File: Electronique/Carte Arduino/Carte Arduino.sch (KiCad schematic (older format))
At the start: 2 parts

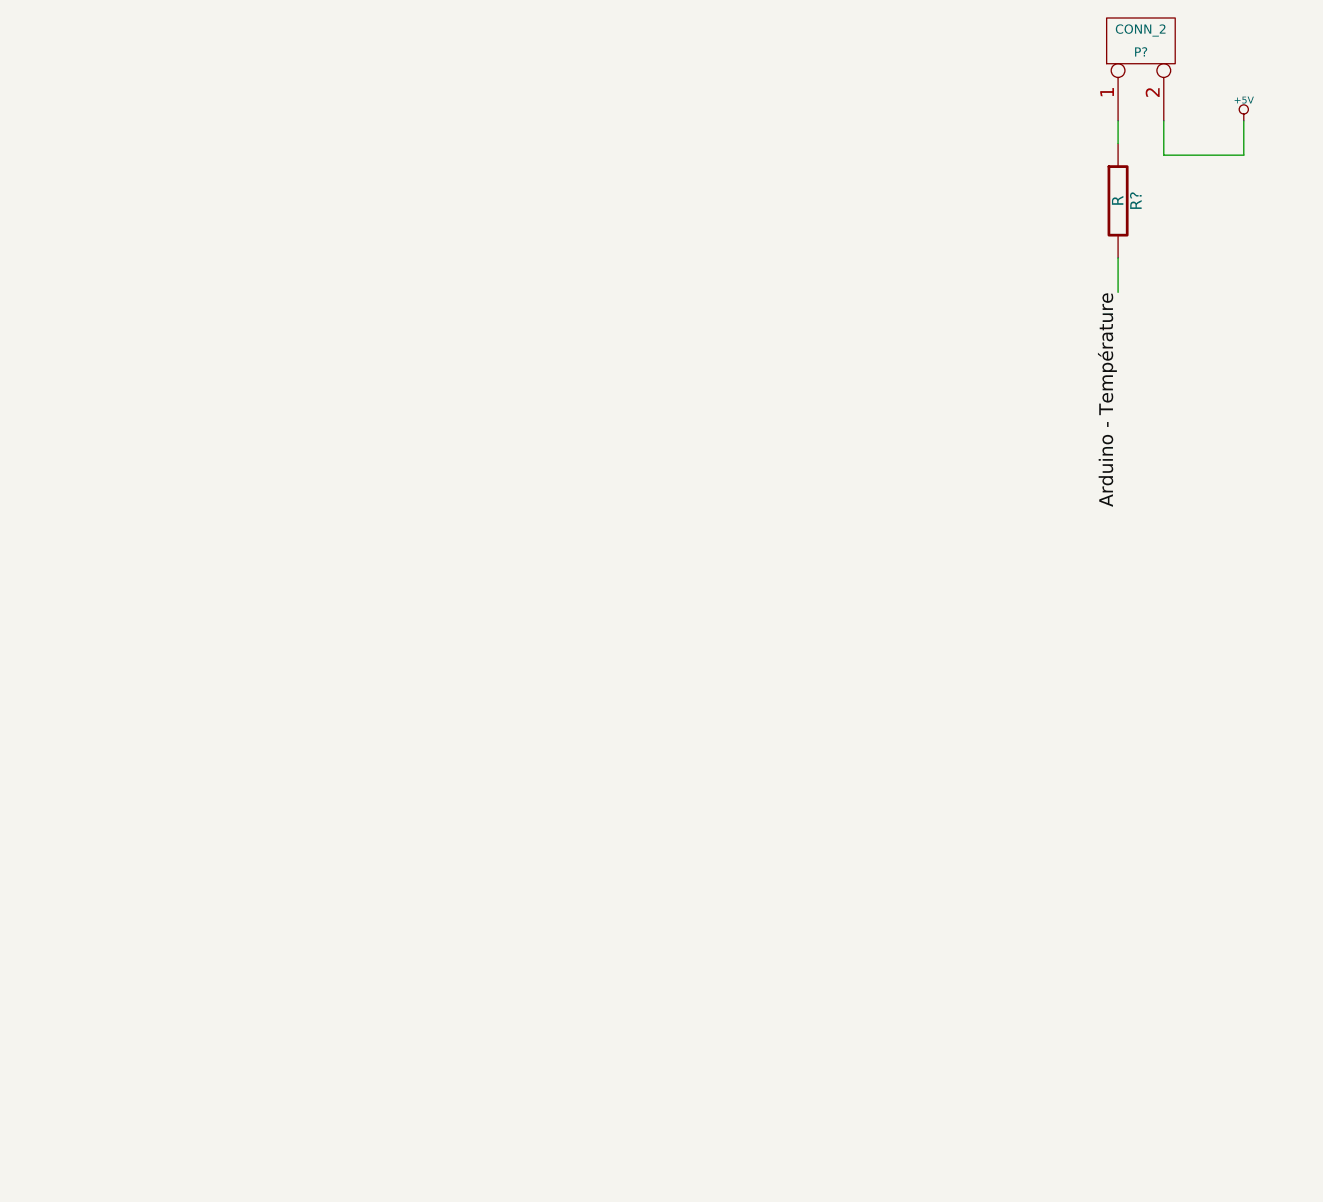
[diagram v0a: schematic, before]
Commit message: Electronique/Carte Arduino/Carte Arduino.sch : - Ajout du capteur de pression
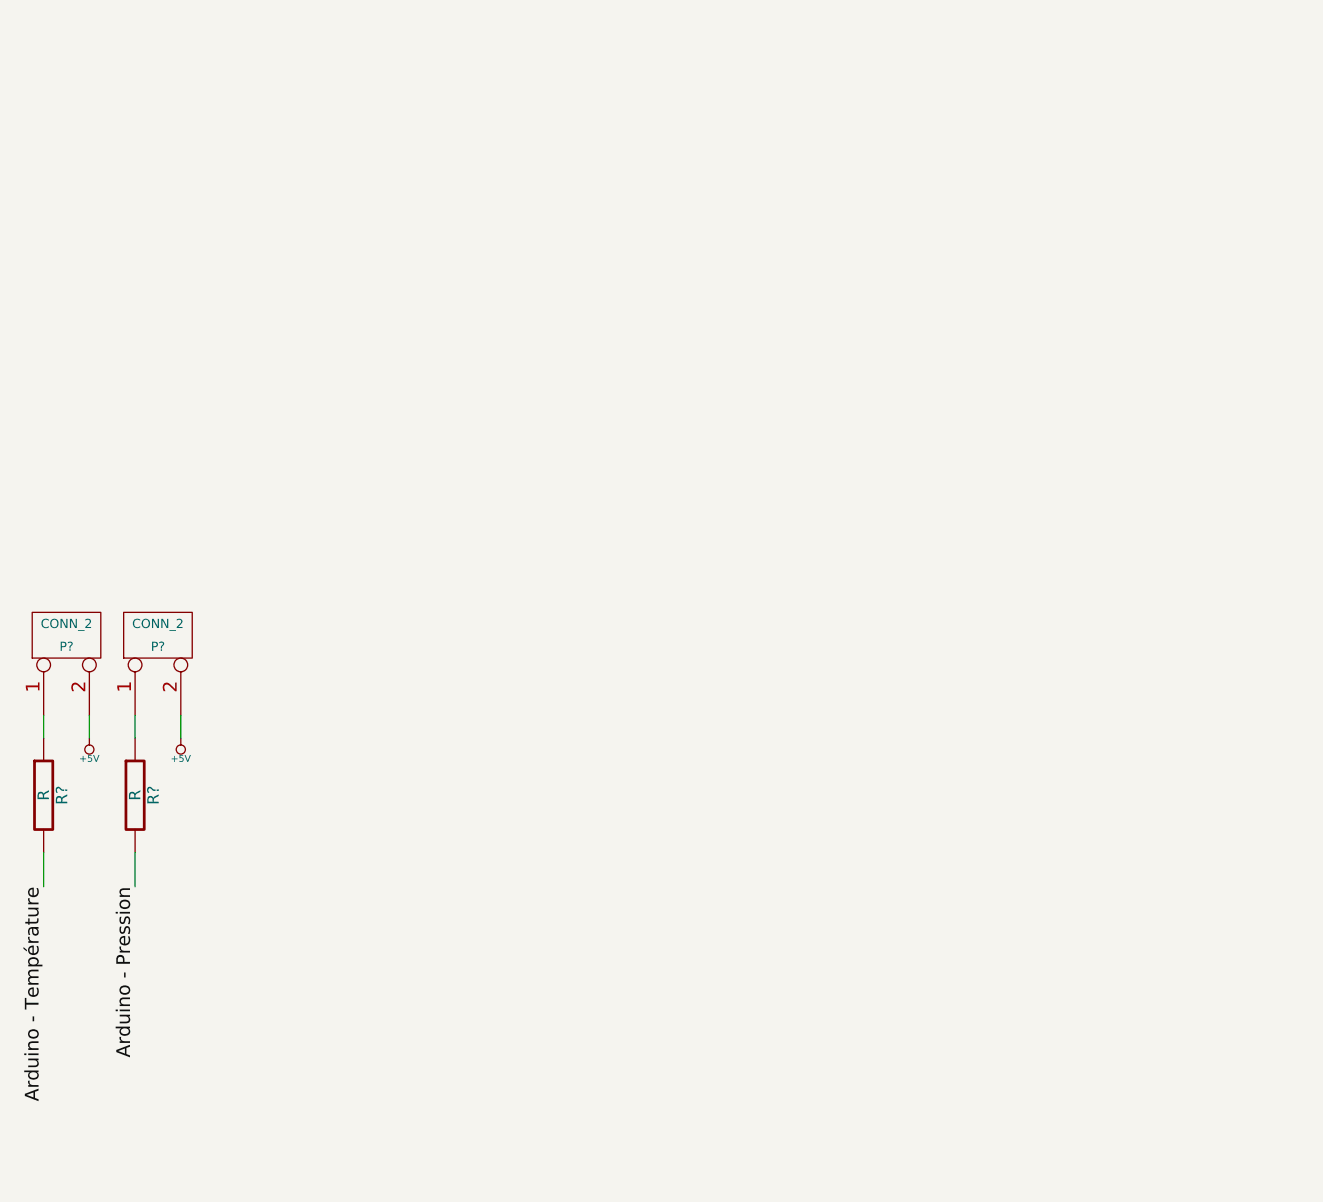
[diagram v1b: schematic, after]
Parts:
- added P?: CONN_2, symbol CONN_2
- added R?: R, symbol R
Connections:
- net +5V: now also P?.2 (PM)
- new net: P?.1 (P1), R?.1
- new net Arduino - Pression: R?.2
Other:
- moved on the sheet: P?, R?
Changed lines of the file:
@@
-EESchema Schematic File Version 2  date 09/12/2011 07:44:42
+EESchema Schematic File Version 2  date 09/12/2011 16:36:29
 LIBS:power
 LIBS:device
@@
 $EndDescr
 Wire Wire Line
-	5550 3450 5550 3600
+	1250 6050 1250 6200
 Wire Wire Line
-	5750 2850 5750 3000
+	1250 5450 1250 5550
 Wire Wire Line
-	5750 3000 6100 3000
+	1450 5550 1450 5450
 Wire Wire Line
-	6100 3000 6100 2850
+	1050 5550 1050 5450
 Wire Wire Line
-	5550 2850 5550 2950
+	850  5450 850  5550
+Wire Wire Line
+	850  6050 850  6200
+$Comp
+L +5V #PWR?
+U 1 1 4EE22ACD
+P 1450 5550
+F 0 "#PWR?" H 1450 5640 20  0001 C CNN
+F 1 "+5V" H 1450 5640 30  0000 C CNN
+	1    1450 5550
+	-1   0    0    1
+$EndComp
+$Comp
+L CONN_2 P?
+U 1 1 4EE22ACC
+P 1350 5100
+F 0 "P?" V 1300 5100 40  0000 C CNN
+F 1 "CONN_2" V 1400 5100 40  0000 C CNN
+	1    1350 5100
+	0    -1   -1   0
+$EndComp
+Text Label 1250 6200 3    60   ~ 0
+Arduino - Pression
+$Comp
+L R R?
+U 1 1 4EE22ACB
+P 1250 5800
+F 0 "R?" V 1330 5800 50  0000 C CNN
+F 1 "R" V 1250 5800 50  0000 C CNN
+	1    1250 5800
+	1    0    0    -1
+$EndComp
 $Comp
 L R R?
 U 1 1 4EE1ADE8
-P 5550 3200
-F 0 "R?" V 5630 3200 50  0000 C CNN
-F 1 "R" V 5550 3200 50  0000 C CNN
-	1    5550 3200
+P 850 5800
+F 0 "R?" V 930 5800 50  0000 C CNN
+F 1 "R" V 850 5800 50  0000 C CNN
+	1    850  5800
 	1    0    0    -1
 $EndComp
-Text Label 5550 3600 3    60   ~ 0
+Text Label 850  6200 3    60   ~ 0
 Arduino - Température
 $Comp
 L CONN_2 P?
 U 1 1 4EE1AD34
-P 5650 2500
-F 0 "P?" V 5600 2500 40  0000 C CNN
-F 1 "CONN_2" V 5700 2500 40  0000 C CNN
-	1    5650 2500
+P 950 5100
+F 0 "P?" V 900 5100 40  0000 C CNN
+F 1 "CONN_2" V 1000 5100 40  0000 C CNN
+	1    950  5100
 	0    -1   -1   0
 $EndComp
@@
 L +5V #PWR?
 U 1 1 4EE0BB2B
-P 6100 2850
-F 0 "#PWR?" H 6100 2940 20  0001 C CNN
-F 1 "+5V" H 6100 2940 30  0000 C CNN
-	1    6100 2850
-	1    0    0    -1
+P 1050 5550
+F 0 "#PWR?" H 1050 5640 20  0001 C CNN
+F 1 "+5V" H 1050 5640 30  0000 C CNN
+	1    1050 5550
+	-1   0    0    1
 $EndComp
 $EndSCHEMATC

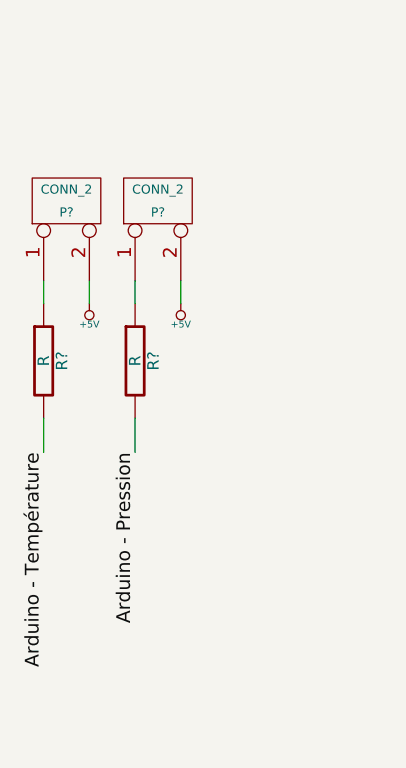
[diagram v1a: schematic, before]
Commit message: Electronique/Carte Arduino/Carte Arduino.pro : - Ajout des capteur de pression et de temperature interne
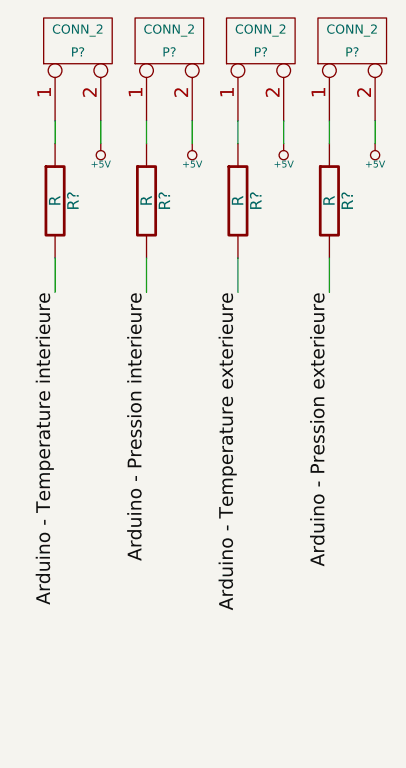
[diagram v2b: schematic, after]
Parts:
- added P? (x2): CONN_2, symbol CONN_2
- added R? (x2): R, symbol R
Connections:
- net +5V: now also P?.2 (PM), P?.2 (PM)
- net Arduino - Pression renamed Arduino - Pression interieure
- net Arduino - Température renamed Arduino - Temperature interieure
- new net: P?.1 (P1), R?.1 (x2)
- new net Arduino - Pression exterieure: R?.2
- new net Arduino - Temperature exterieure: R?.2
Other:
- moved on the sheet: P?, R?
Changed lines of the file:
@@
-EESchema Schematic File Version 2  date 09/12/2011 16:36:29
-LIBS:power
-LIBS:device
-LIBS:transistors
-LIBS:conn
-LIBS:linear
-LIBS:regul
-LIBS:74xx
-LIBS:cmos4000
-LIBS:adc-dac
-LIBS:memory
-LIBS:xilinx
-LIBS:special
-LIBS:microcontrollers
-LIBS:dsp
-LIBS:microchip
-LIBS:analog_switches
-LIBS:motorola
-LIBS:texas
-LIBS:intel
-LIBS:audio
-LIBS:interface
-LIBS:digital-audio
-LIBS:philips
-LIBS:display
-LIBS:cypress
-LIBS:siliconi
-LIBS:opto
-LIBS:atmel
-LIBS:contrib
-LIBS:valves
-LIBS:Carte Arduino-cache
-EELAYER 25  0
+EESchema Schematic File Version 1
+LIBS:power,device,conn,linear,regul,74xx,cmos4000,adc-dac,memory,xilinx,special,microcontrollers,dsp,microchip,analog_switches,motorola,texas,intel,audio,interface,digital-audio,philips,display,cypress,siliconi,contrib,valves
+EELAYER 23  0
 EELAYER END
 $Descr A4 11700 8267
-encoding utf-8
 Sheet 1 1
 Title ""
@@
 $EndDescr
 Wire Wire Line
-	1250 6050 1250 6200
+	2100 5350 2100 5500
 Wire Wire Line
-	1250 5450 1250 5550
+	2100 4750 2100 4850
 Wire Wire Line
-	1450 5550 1450 5450
+	2300 4850 2300 4750
 Wire Wire Line
-	1050 5550 1050 5450
+	1900 4850 1900 4750
 Wire Wire Line
-	850  5450 850  5550
+	1700 4750 1700 4850
 Wire Wire Line
-	850  6050 850  6200
+	1700 5350 1700 5500
+$Comp
+L +5V #PWR?
+U 1 1 4EE364FB
+P 2300 4850
+F 0 "#PWR?" H 2300 4940 20  0001 C C
+F 1 "+5V" H 2300 4940 30  0000 C C
+	1    2300 4850
+	-1   0    0    1
+$EndComp
+$Comp
+L CONN_2 P?
+U 1 1 4EE364FA
+P 2200 4400
+F 0 "P?" V 2150 4400 40  0000 C C
+F 1 "CONN_2" V 2250 4400 40  0000 C C
+	1    2200 4400
+	0    -1   -1   0
+$EndComp
+Text Label 2100 5500 3    60   ~
+Arduino - Pression exterieure
+$Comp
+L R R?
+U 1 1 4EE364F9
+P 2100 5100
+F 0 "R?" V 2180 5100 50  0000 C C
+F 1 "R" V 2100 5100 50  0000 C C
+	1    2100 5100
+	1    0    0    -1
+$EndComp
+$Comp
+L R R?
+U 1 1 4EE364F8
+P 1700 5100
+F 0 "R?" V 1780 5100 50  0000 C C
+F 1 "R" V 1700 5100 50  0000 C C
+	1    1700 5100
+	1    0    0    -1
+$EndComp
+Text Label 1700 5500 3    60   ~
+Arduino - Temperature exterieure
+$Comp
+L CONN_2 P?
+U 1 1 4EE364F7
+P 1800 4400
+F 0 "P?" V 1750 4400 40  0000 C C
+F 1 "CONN_2" V 1850 4400 40  0000 C C
+	1    1800 4400
+	0    -1   -1   0
+$EndComp
+$Comp
+L +5V #PWR?
+U 1 1 4EE364F6
+P 1900 4850
+F 0 "#PWR?" H 1900 4940 20  0001 C C
+F 1 "+5V" H 1900 4940 30  0000 C C
+	1    1900 4850
+	-1   0    0    1
+$EndComp
+Wire Wire Line
+	1300 5350 1300 5500
+Wire Wire Line
+	1300 4750 1300 4850
+Wire Wire Line
+	1500 4850 1500 4750
+Wire Wire Line
+	1100 4850 1100 4750
+Wire Wire Line
+	900  4750 900  4850
+Wire Wire Line
+	900  5350 900  5500
 $Comp
 L +5V #PWR?
 U 1 1 4EE22ACD
-P 1450 5550
-F 0 "#PWR?" H 1450 5640 20  0001 C CNN
-F 1 "+5V" H 1450 5640 30  0000 C CNN
-	1    1450 5550
+P 1500 4850
+F 0 "#PWR?" H 1500 4940 20  0001 C C
+F 1 "+5V" H 1500 4940 30  0000 C C
+	1    1500 4850
 	-1   0    0    1
 $EndComp
@@
 L CONN_2 P?
 U 1 1 4EE22ACC
-P 1350 5100
-F 0 "P?" V 1300 5100 40  0000 C CNN
-F 1 "CONN_2" V 1400 5100 40  0000 C CNN
-	1    1350 5100
+P 1400 4400
+F 0 "P?" V 1350 4400 40  0000 C C
+F 1 "CONN_2" V 1450 4400 40  0000 C C
+	1    1400 4400
 	0    -1   -1   0
 $EndComp
-Text Label 1250 6200 3    60   ~ 0
-Arduino - Pression
+Text Label 1300 5500 3    60   ~
+Arduino - Pression interieure
 $Comp
 L R R?
 U 1 1 4EE22ACB
-P 1250 5800
-F 0 "R?" V 1330 5800 50  0000 C CNN
-F 1 "R" V 1250 5800 50  0000 C CNN
-	1    1250 5800
+P 1300 5100
+F 0 "R?" V 1380 5100 50  0000 C C
+F 1 "R" V 1300 5100 50  0000 C C
+	1    1300 5100
 	1    0    0    -1
 $EndComp
@@
 L R R?
 U 1 1 4EE1ADE8
-P 850 5800
-F 0 "R?" V 930 5800 50  0000 C CNN
-F 1 "R" V 850 5800 50  0000 C CNN
-	1    850  5800
+P 900 5100
+F 0 "R?" V 980 5100 50  0000 C C
+F 1 "R" V 900 5100 50  0000 C C
+	1    900  5100
 	1    0    0    -1
 $EndComp
-Text Label 850  6200 3    60   ~ 0
-Arduino - Température
+Text Label 900  5500 3    60   ~
+Arduino - Temperature interieure
 $Comp
 L CONN_2 P?
 U 1 1 4EE1AD34
-P 950 5100
-F 0 "P?" V 900 5100 40  0000 C CNN
-F 1 "CONN_2" V 1000 5100 40  0000 C CNN
-	1    950  5100
+P 1000 4400
+F 0 "P?" V 950 4400 40  0000 C C
+F 1 "CONN_2" V 1050 4400 40  0000 C C
+	1    1000 4400
 	0    -1   -1   0
 $EndComp
@@
 L +5V #PWR?
 U 1 1 4EE0BB2B
-P 1050 5550
-F 0 "#PWR?" H 1050 5640 20  0001 C CNN
-F 1 "+5V" H 1050 5640 30  0000 C CNN
-	1    1050 5550
+P 1100 4850
+F 0 "#PWR?" H 1100 4940 20  0001 C C
+F 1 "+5V" H 1100 4940 30  0000 C C
+	1    1100 4850
 	-1   0    0    1
 $EndComp
